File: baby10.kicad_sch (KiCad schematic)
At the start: 59 parts, among them J1 Barrel_Jack_Switch, J2 Euro_Power, J3 Clock_In, J4 Clock_Out, J5 OUT, SW1 Run, SW2 SW_8pos, U1 LM555xN, U2 4017

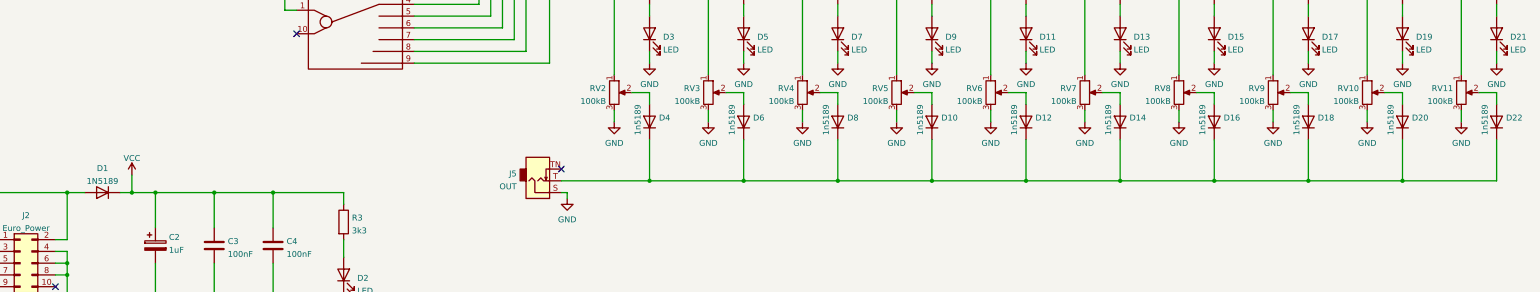
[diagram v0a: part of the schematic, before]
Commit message: Change diodes
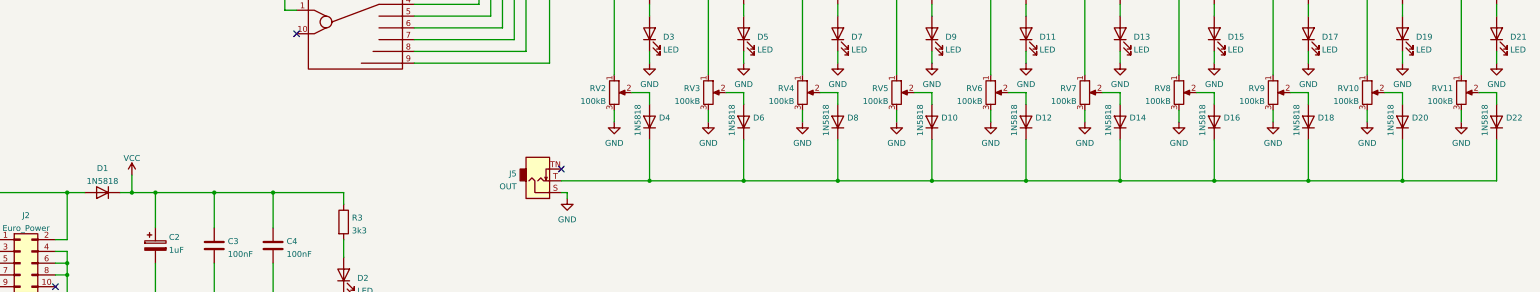
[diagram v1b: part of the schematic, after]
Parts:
- D1: value 1N5189 -> 1N5818
- D10, D12, D14, D16, D18, D20, D22, D4, D6, D8: value 1n5189 -> 1N5818
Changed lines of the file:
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@@
       (effects (font (size 1.27 1.27)) (justify right))
     )
-    (property "Value" "1n5189" (id 1) (at 335.28 218.44 0)
+    (property "Value" "1N5818" (id 1) (at 335.28 218.44 0)
       (effects (font (size 1.27 1.27)) (justify right))
     )
@@
       (effects (font (size 1.27 1.27)) (justify right))
     )
-    (property "Value" "1n5189" (id 1) (at 193.04 218.44 0)
+    (property "Value" "1N5818" (id 1) (at 193.04 218.44 0)
       (effects (font (size 1.27 1.27)) (justify right))
     )
@@
       (effects (font (size 1.27 1.27)) (justify right))
     )
-    (property "Value" "1n5189" (id 1) (at 213.36 218.44 0)
+    (property "Value" "1N5818" (id 1) (at 213.36 218.44 0)
       (effects (font (size 1.27 1.27)) (justify right))
     )
@@
     (in_bom yes) (on_board yes) (fields_autoplaced)
     (property "Reference" "D1" (id 0) (at 77.47 232.2535 0))
-    (property "Value" "1N5189" (id 1) (at 77.47 235.0286 0))
+    (property "Value" "1N5818" (id 1) (at 77.47 235.0286 0))
     (property "Footprint" "Rumblesan_Footprints:D_DO-35_SOD27_P7.62mm_Horizontal" (id 2) (at 77.47 237.49 0)
       (effects (font (size 1.27 1.27)) hide)
@@
       (effects (font (size 1.27 1.27)) (justify right))
     )
-    (property "Value" "1n5189" (id 1) (at 233.68 218.44 0)
+    (property "Value" "1N5818" (id 1) (at 233.68 218.44 0)
       (effects (font (size 1.27 1.27)) (justify right))
     )
@@
       (effects (font (size 1.27 1.27)) (justify right))
     )
-    (property "Value" "1n5189" (id 1) (at 254 218.44 0)
+    (property "Value" "1N5818" (id 1) (at 254 218.44 0)
       (effects (font (size 1.27 1.27)) (justify right))
     )
@@
       (effects (font (size 1.27 1.27)) (justify right))
     )
-    (property "Value" "1n5189" (id 1) (at 294.64 218.44 0)
+    (property "Value" "1N5818" (id 1) (at 294.64 218.44 0)
       (effects (font (size 1.27 1.27)) (justify right))
     )
@@
       (effects (font (size 1.27 1.27)) (justify right))
     )
-    (property "Value" "1n5189" (id 1) (at 274.32 218.44 0)
+    (property "Value" "1N5818" (id 1) (at 274.32 218.44 0)
       (effects (font (size 1.27 1.27)) (justify right))
     )
@@
       (effects (font (size 1.27 1.27)) (justify right))
     )
-    (property "Value" "1n5189" (id 1) (at 314.96 218.44 0)
+    (property "Value" "1N5818" (id 1) (at 314.96 218.44 0)
       (effects (font (size 1.27 1.27)) (justify right))
     )
@@
       (effects (font (size 1.27 1.27)) (justify right))
     )
-    (property "Value" "1n5189" (id 1) (at 355.6 218.44 0)
+    (property "Value" "1N5818" (id 1) (at 355.6 218.44 0)
       (effects (font (size 1.27 1.27)) (justify right))
     )
@@
       (effects (font (size 1.27 1.27)) (justify right))
     )
-    (property "Value" "1n5189" (id 1) (at 375.92 218.44 0)
+    (property "Value" "1N5818" (id 1) (at 375.92 218.44 0)
       (effects (font (size 1.27 1.27)) (justify right))
     )
@@
     )
     (path "/5e2513d9-6d2b-4041-b62c-804d4997e6f7"
-      (reference "D1") (unit 1) (value "1N5189") (footprint "Rumblesan_Footprints:D_DO-35_SOD27_P7.62mm_Horizontal")
+      (reference "D1") (unit 1) (value "1N5818") (footprint "Rumblesan_Footprints:D_DO-35_SOD27_P7.62mm_Horizontal")
     )
     (path "/d27579ec-1b2c-4dd4-8c71-2086263c764c"
@@
     )
     (path "/49090e21-2f19-435d-be3d-af6ecb4d54e5"
-      (reference "D4") (unit 1) (value "1n5189") (footprint "Rumblesan_Footprints:D_DO-35_SOD27_P7.62mm_Horizontal")
+      (reference "D4") (unit 1) (value "1N5818") (footprint "Rumblesan_Footprints:D_DO-35_SOD27_P7.62mm_Horizontal")
     )
     (path "/bac01b95-7634-499e-9803-c9cf09f78759"
@@
     )
     (path "/51bd6530-965d-4164-8b1e-e9dd6b9589dd"
-      (reference "D6") (unit 1) (value "1n5189") (footprint "Rumblesan_Footprints:D_DO-35_SOD27_P7.62mm_Horizontal")
+      (reference "D6") (unit 1) (value "1N5818") (footprint "Rumblesan_Footprints:D_DO-35_SOD27_P7.62mm_Horizontal")
     )
     (path "/4c3fd6b0-3d7e-4ff0-95ac-346dc03ccc64"
@@
     )
     (path "/5fe0648f-328c-42f7-9d27-20457b731f54"
-      (reference "D8") (unit 1) (value "1n5189") (footprint "Rumblesan_Footprints:D_DO-35_SOD27_P7.62mm_Horizontal")
+      (reference "D8") (unit 1) (value "1N5818") (footprint "Rumblesan_Footprints:D_DO-35_SOD27_P7.62mm_Horizontal")
     )
     (path "/d4df4617-012f-453b-a3a0-52cce1fbb056"
@@
     )
     (path "/6283f04c-40df-43c9-9950-fec8685049b3"
-      (reference "D10") (unit 1) (value "1n5189") (footprint "Rumblesan_Footprints:D_DO-35_SOD27_P7.62mm_Horizontal")
+      (reference "D10") (unit 1) (value "1N5818") (footprint "Rumblesan_Footprints:D_DO-35_SOD27_P7.62mm_Horizontal")
     )
     (path "/4f004101-8740-4a28-a9a0-4d0b83ef11e0"
@@
     )
     (path "/b83affa2-90d9-40aa-a552-2dea25375059"
-      (reference "D12") (unit 1) (value "1n5189") (footprint "Rumblesan_Footprints:D_DO-35_SOD27_P7.62mm_Horizontal")
+      (reference "D12") (unit 1) (value "1N5818") (footprint "Rumblesan_Footprints:D_DO-35_SOD27_P7.62mm_Horizontal")
     )
     (path "/3d8b32e4-e9c7-481c-8b97-db15c9136302"
@@
     )
     (path "/6543790b-43f1-4bf8-b91c-869329e518dc"
-      (reference "D14") (unit 1) (value "1n5189") (footprint "Rumblesan_Footprints:D_DO-35_SOD27_P7.62mm_Horizontal")
+      (reference "D14") (unit 1) (value "1N5818") (footprint "Rumblesan_Footprints:D_DO-35_SOD27_P7.62mm_Horizontal")
     )
     (path "/8fe4ec95-6293-45da-ad84-985f95d8d041"
@@
     )
     (path "/bfb2a1d8-cf55-4a8f-889d-09edd1040e21"
-      (reference "D16") (unit 1) (value "1n5189") (footprint "Rumblesan_Footprints:D_DO-35_SOD27_P7.62mm_Horizontal")
+      (reference "D16") (unit 1) (value "1N5818") (footprint "Rumblesan_Footprints:D_DO-35_SOD27_P7.62mm_Horizontal")
     )
     (path "/0f5e253a-8150-4eac-8447-3f17031f3de2"
@@
     )
     (path "/2d5677d4-74ce-44d9-9194-1110ab58e2ed"
-      (reference "D18") (unit 1) (value "1n5189") (footprint "Rumblesan_Footprints:D_DO-35_SOD27_P7.62mm_Horizontal")
+      (reference "D18") (unit 1) (value "1N5818") (footprint "Rumblesan_Footprints:D_DO-35_SOD27_P7.62mm_Horizontal")
     )
     (path "/7fd3fd1f-2f4e-4a03-aa97-4453537359d3"
@@
     )
     (path "/ca12990e-7f45-43ac-9e1f-b221895a5a7c"
-      (reference "D20") (unit 1) (value "1n5189") (footprint "Rumblesan_Footprints:D_DO-35_SOD27_P7.62mm_Horizontal")
+      (reference "D20") (unit 1) (value "1N5818") (footprint "Rumblesan_Footprints:D_DO-35_SOD27_P7.62mm_Horizontal")
     )
     (path "/cccfef4b-a53b-4fc6-b32c-13903a6a7563"
@@
     )
     (path "/cf5bbf0d-c4a0-4079-baac-23e20f9c0648"
-      (reference "D22") (unit 1) (value "1n5189") (footprint "Rumblesan_Footprints:D_DO-35_SOD27_P7.62mm_Horizontal")
+      (reference "D22") (unit 1) (value "1N5818") (footprint "Rumblesan_Footprints:D_DO-35_SOD27_P7.62mm_Horizontal")
     )
     (path "/f7dc1e09-a0e1-4e6d-9e54-0975b557c666"
